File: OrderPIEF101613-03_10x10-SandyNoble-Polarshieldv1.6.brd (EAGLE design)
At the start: 100 x 80 mm, 62 parts, among them CN1 1X4-CLEANBIG, CN2 1X4-CLEANBIG, J1 1X2-3.5MM, U1 ARDUINO_MEGA_SHIELD, X1 2.1MMJACKTHM

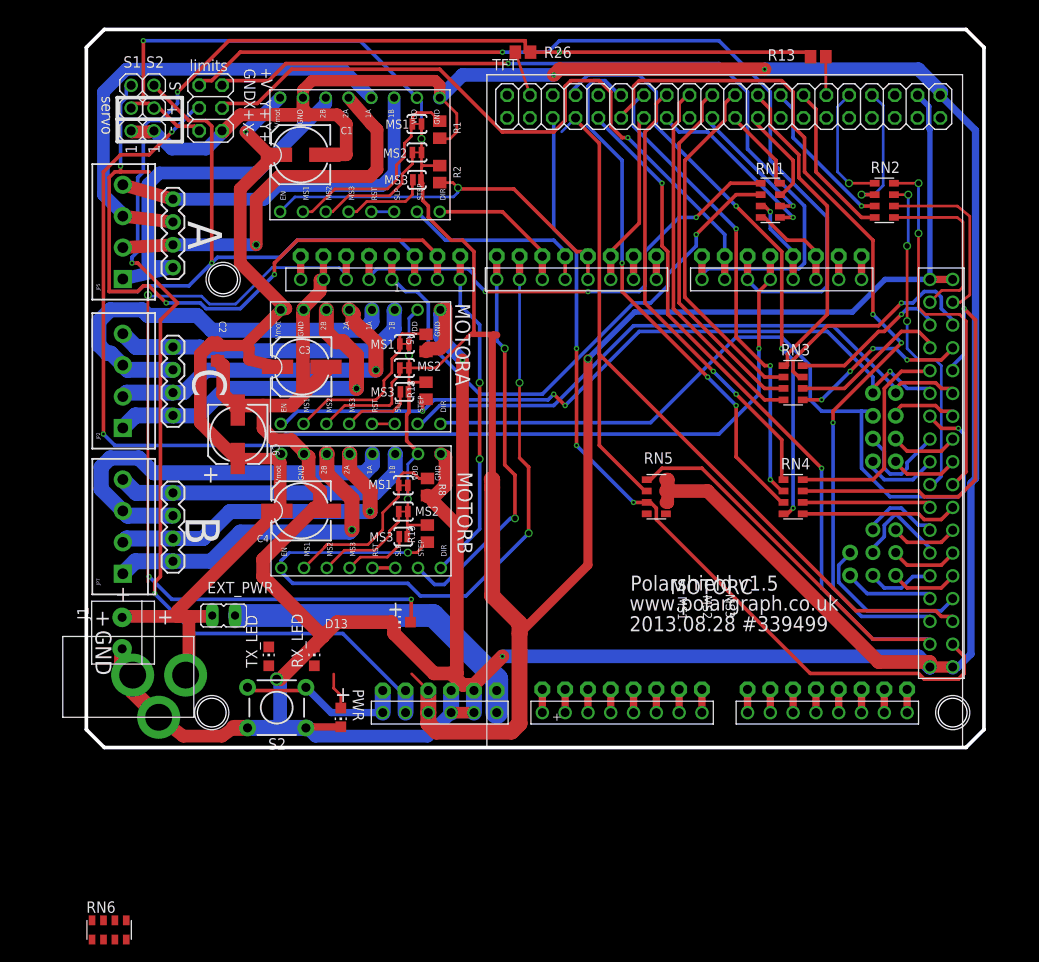
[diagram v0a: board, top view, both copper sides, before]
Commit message: Merged a resistor into a network and changed a few values, also cleaned up silkscreen.
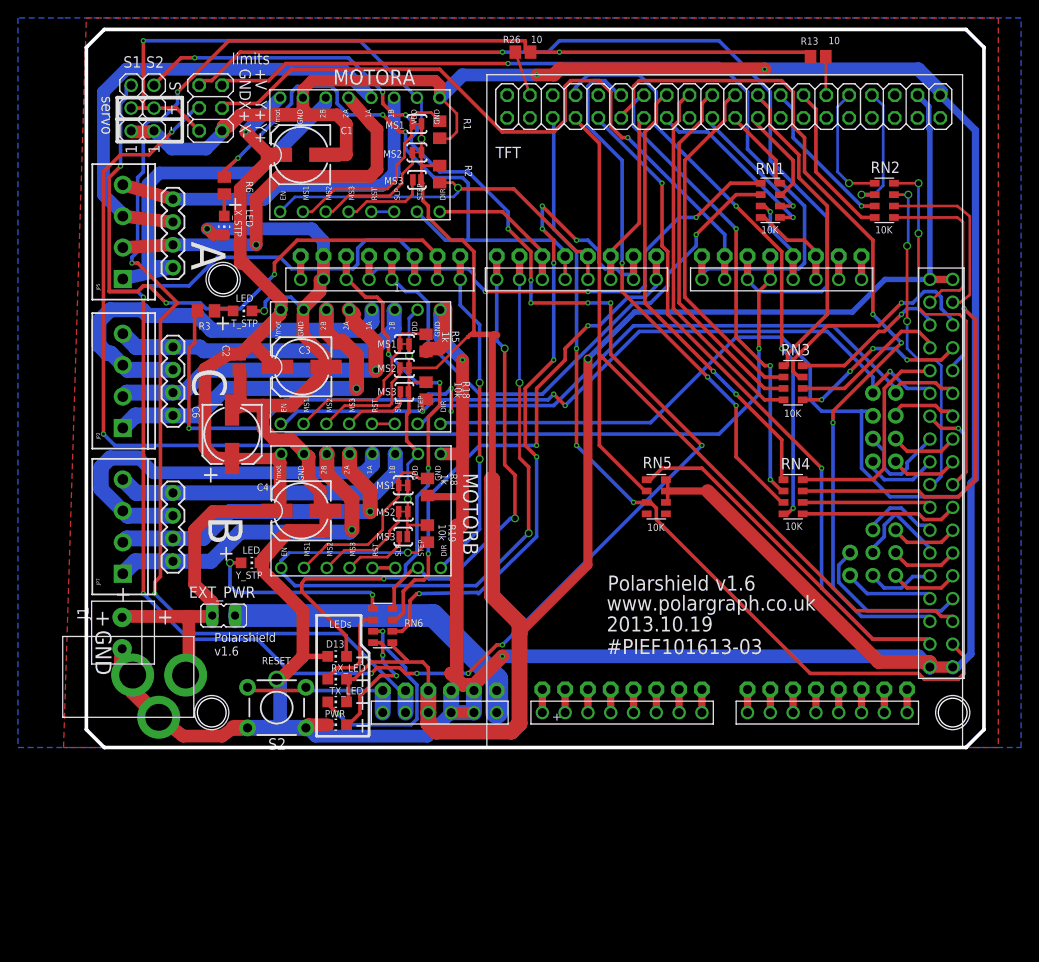
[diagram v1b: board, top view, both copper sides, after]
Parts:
- added R3: 1K, rcl:R0805
- added R6: 1k, rcl:R0805
- added T_STP, X_STP, Y_STP: (no value), led:CHIP-LED0805
- R1, R5, R8: value 100k -> 1k
- moved RN6 45.6 mm to (33.0, 13.6), turned to 270 degrees
- moved TX_LED 9.16 mm to (27.9, 5.08), turned to 90 degrees
- moved D13 8.07 mm to (27.9, 10.2)
- moved RX_LED 3.59 mm to (27.9, 7.62), turned to 90 degrees
- moved C2 2.62 mm to (17.0, 42.9)
- moved PWR 0.91 mm to (27.9, 2.54), turned to 90 degrees
- moved C6 0.63 mm to (16.2, 34.9)
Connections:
- net T-DIR renamed X-DIR
- net T-EN renamed X-EN
- removed net T-STEP: CN1.4, U$6.STEP, U1.D31
- new net N$23: R3.1, T_STP.A
- new net X-STEP: CN1.4, R3.2, U$6.STEP, U1.D31
- net GND: now also T_STP.C, X_STP.C, Y_STP.C
- net N$15: now also RN6.2, RX_LED.C; no longer TX_LED.C
- net N$16: now also RN6.3, TX_LED.C; no longer RX_LED.C
- net N$18: now also RN6.1, Y_STP.A; no longer RN6.3, TX_LED.A
- net N$19: now also R6.1, X_STP.A; no longer RN6.2, RX_LED.A
- net N$2: now also RN6.4; no longer RN6.1
- net VCC: now also RN6.5, RX_LED.A, TX_LED.A; no longer RN6.8
- net Y-STEP: now also RN6.8
- net Z-STEP: now also R6.2
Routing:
- net SERV2: track 63.3 -> 243.5 mm, vias 1 -> 15
- net X-STEP: track 0.00 -> 116.8 mm, vias 0 -> 3
- net D1: track 2.59 -> 78.3 mm, vias 0 -> 7
- net T-STEP: track 69.1 -> 0.00 mm
- net D0: track 2.59 -> 59.1 mm, vias 0 -> 3
- net Z-STEP: track 21.4 -> 66.6 mm, vias 0 -> 3
- net LED: track 92.7 -> 66.7 mm, vias 3 -> 4
- net N$16: track 0.00 -> 24.1 mm, vias 0 -> 2
- net N$18: track 0.00 -> 21.7 mm, vias 0 -> 2
- net VCC: track 291.5 -> 306.5 mm
- net N$15: track 0.00 -> 10.7 mm
- net N$2: track 4.11 -> 14.2 mm, vias 0 -> 2
- net Y-STEP: track 44.7 -> 50.4 mm
- net SERV1: track 73.4 -> 69.9 mm
- net N$19: track 0.00 -> 2.96 mm
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- added copper zone on layer 1, net GND
- added copper zone on layer 16, net GND
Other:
- board text added: "10"
- board text added: "10K"
- board text added: "10k"
- board text added: "1k"
- board text added: "2013.10.19 #PIEF101613-03"
- board text added: "LED"
- board text added: "LEDs"
- board text added: "Polarshield v1.6"
- board text added: "RESET"
- board text removed: "2013.08.28 #339499"
- board text removed: "MOTORC"
- board text removed: "Polarshield v1.5"
